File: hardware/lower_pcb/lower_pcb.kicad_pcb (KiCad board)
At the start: 2 copper layers, 88 x 88 mm, 4 parts

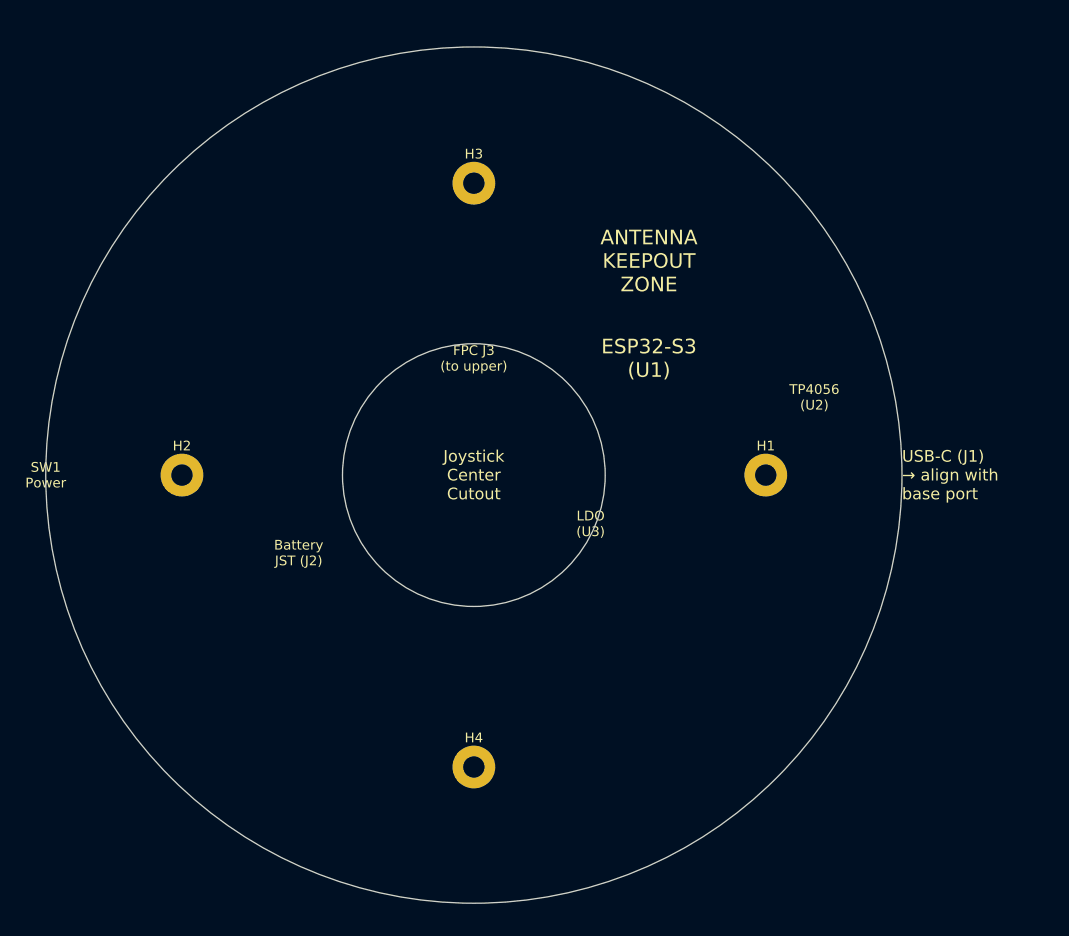
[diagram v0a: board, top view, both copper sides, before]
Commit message: feat: KiCad PCB files with full netlist and copper traces
lower_pcb.kicad_pcb (rev 2.4):
- All pads with correct net assignments
- 91 trace segments/vias covering all nets:
  3V3 rail, GND pour taps, VBUS, BAT_PLUS, SW_OUT (LDO)
  JOY_X/Y/SW from XIAO to Alps RKJXV pads
  BTN_L/R/BK/FW from XIAO to FPC J3 pins
  BT_SYNC from XIAO to SW_BT + R_PU_BT
  BAT_PLUS on B.Cu from J2 to SW1
- Via to B.Cu for J2 battery connector routing

upper_pcb.kicad_pcb (rev 1.6):
- All pads: SW4/SW5 GM8.0 THT, SW6/SW7 Blue Dot SMD, R1-R4, C1, J5 FPC on B.Cu
- 52 trace segments/vias:
  3V3 rail via from J5 B.Cu through to F.Cu R1-R4 pull-ups
  GND rail to all switch COM/GND pads and C1
  BTN_L/R via FPC->pull-up->switch signal pad for all 4 buttons

Open in KiCad 7, run DRC, fix any remaining unrouted connections with interactive router
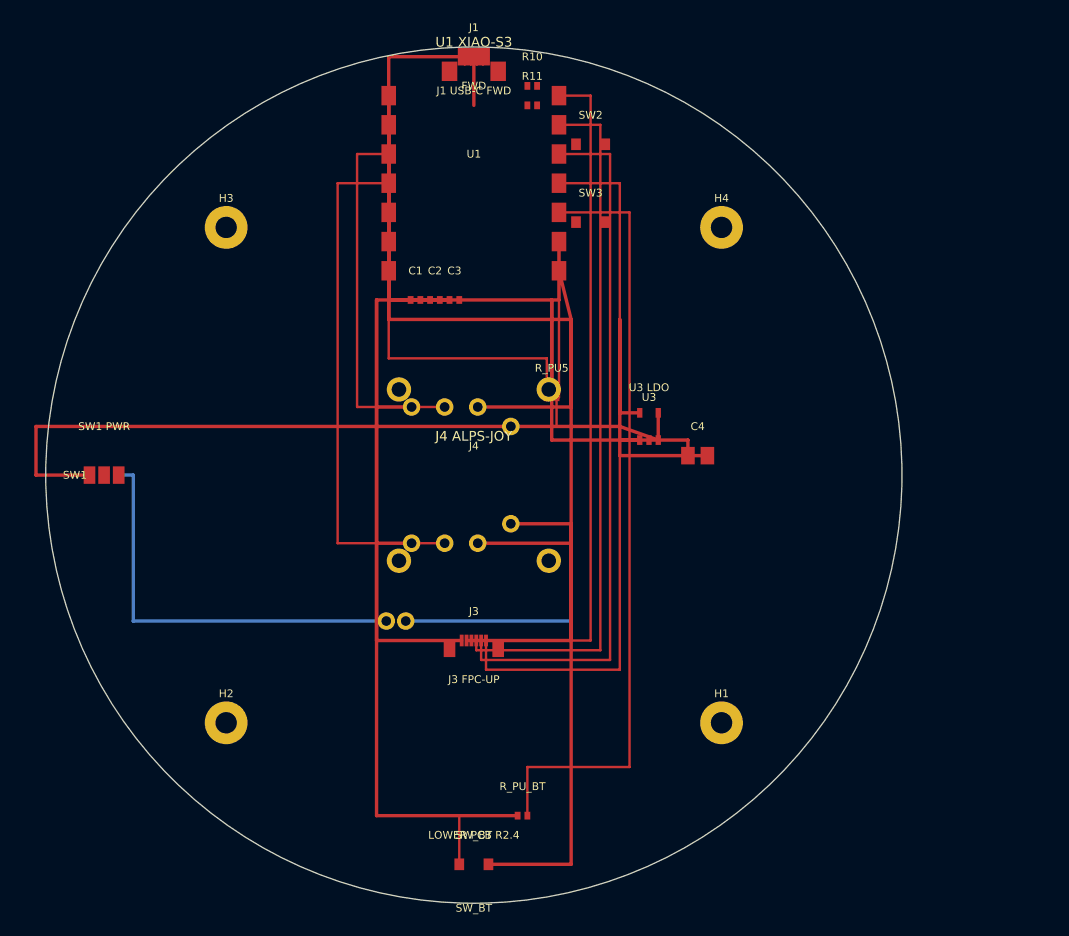
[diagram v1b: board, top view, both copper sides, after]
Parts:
- added C1: R-0402, C1, F.Cu at (94.0, 82.0)
- added C2: R-0402, C2, F.Cu at (96.0, 82.0)
- added C3: R-0402, C3, F.Cu at (98.0, 82.0)
- added C4: C-0805, C4, F.Cu at (123.0, 98.0)
- added J1: USB-C, J1, F.Cu at (100.0, 57.0)
- added J2: JST-PH-2P, J2, B.Cu at (92.0, 115.0)
- added J3: FPC-6P-0.5mm, J3, F.Cu at (100.0, 117.0)
- added J4: Alps-RKJXV, J4, F.Cu at (100.0, 100.0)
- added R10: R-0402, R10, F.Cu at (106.0, 60.0)
- added R11: R-0402, R11, F.Cu at (106.0, 62.0)
- added R_PU5: R-0402, R_PU5, F.Cu at (108.0, 92.0)
- added R_PU_BT: R-0402, R_PU_BT, F.Cu at (105.0, 135.0)
- added SW1: MSK-12C02, SW1, F.Cu at (62.0, 100.0)
- added SW2: BOOT-SW, SW2, F.Cu at (112.0, 66.0)
- added SW3: RESET-SW, SW3, F.Cu at (112.0, 74.0)
- added SW_BT: BT-SYNC-SW, SW_BT, F.Cu at (100.0, 140.0)
- added U1: XIAO-ESP32S3, U1, F.Cu at (100.0, 70.0)
- added U3: AP2112K-3.3V, U3, F.Cu at (118.0, 95.0)
- H1: value MountingHole_M2 -> M2-Mount; footprint MountingHole:MountingHole_2.2mm_M2_Pad -> H1
- H2: value MountingHole_M2 -> M2-Mount; footprint MountingHole:MountingHole_2.2mm_M2_Pad -> H2
- H3: value MountingHole_M2 -> M2-Mount; footprint MountingHole:MountingHole_2.2mm_M2_Pad -> H3
- H4: value MountingHole_M2 -> M2-Mount; footprint MountingHole:MountingHole_2.2mm_M2_Pad -> H4
- moved H4 61.0 mm to (125.5, 74.5)
- moved H1 25.9 mm to (125.5, 125.5)
- moved H2 25.9 mm to (74.5, 125.5)
- moved H3 25.9 mm to (74.5, 74.5)
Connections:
- H1 pad 1: (no net) -> GND
- H2 pad 1: (no net) -> GND
- H3 pad 1: (no net) -> GND
- H4 pad 1: (no net) -> GND
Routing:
- net GND: track 0.00 -> 254.4 mm, vias 0 -> 1
- net 3V3: track 0.00 -> 210.9 mm
- net BT_SYNC: track 0.00 -> 90.8 mm
- net SW_OUT: track 0.00 -> 77.5 mm
- net BTN_FW: track 0.00 -> 73.0 mm
- net BTN_BK: track 0.00 -> 72.5 mm
- net BTN_R: track 0.00 -> 72.0 mm
- net BTN_L: track 0.00 -> 71.5 mm
- net JOY_SW: track 0.00 -> 60.2 mm
- net JOY_Y: track 0.00 -> 53.2 mm
- net BAT_PLUS: track 0.00 -> 42.5 mm
- net JOY_X: track 0.00 -> 38.2 mm
- net VBUS: track 0.00 -> 6.25 mm
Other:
- outline, holes or cut-outs redrawn
- board text added: "FWD"
- board text added: "J1 USB-C FWD"
- board text added: "J2 LIPO"
- board text added: "J3 FPC-UP"
- board text added: "J4 ALPS-JOY"
- board text added: "LOWER PCB R2.4"
- board text added: "SW1 PWR"
- board text added: "SW_BT"
- board text added: "U1 XIAO-S3"
- board text added: "U3 LDO"
- board text removed: "ANTENNA KEEPOUT ZONE"
- board text removed: "Battery JST (J2)"
- board text removed: "ESP32-S3 (U1)"
- board text removed: "FPC J3 (to upper)"
- board text removed: "Joystick Center Cutout"
- board text removed: "LDO (U3)"
- board text removed: "SW1 Power"
- board text removed: "TP4056 (U2)"
- board text removed: "USB-C (J1) → align with base port"
